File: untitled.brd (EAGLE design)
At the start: 42.2 x 28.6 mm, 27 parts, among them IC1 ACS758LCB-050B-PFF-T, IC2 LM2936DT-3.3

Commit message: Update board layout
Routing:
- net N$8: track 36.7 -> 35.9 mm
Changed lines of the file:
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@@
 <wire x1="37.465" y1="23.9219" x2="37.465" y2="24.765" width="0.3048" layer="16"/>
 <wire x1="37.465" y1="24.765" x2="37.912" y2="25.212" width="0.3048" layer="16"/>
-<wire x1="37.912" y1="25.212" x2="40.193" y2="25.212" width="0.3048" layer="16"/>
-<wire x1="40.193" y1="25.212" x2="41.275" y2="24.13" width="0.3048" layer="16"/>
-<wire x1="41.275" y1="24.13" x2="53.34" y2="24.13" width="0.3048" layer="16"/>
+<wire x1="37.912" y1="25.212" x2="38.923" y2="25.212" width="0.3048" layer="16"/>
+<wire x1="38.923" y1="25.212" x2="40.005" y2="24.13" width="0.3048" layer="16"/>
+<wire x1="40.005" y1="24.13" x2="53.34" y2="24.13" width="0.3048" layer="16"/>
 <wire x1="53.34" y1="24.13" x2="53.655" y2="23.815" width="0.3048" layer="16"/>
 <wire x1="53.655" y1="23.815" x2="53.655" y2="22.86" width="0.3048" layer="16"/>
@@
 <wire x1="45.085" y1="25.72" x2="43.18" y2="25.72" width="0.3048" layer="16"/>
 <wire x1="37.965" y1="28.1481" x2="37.965" y2="26.805" width="0.3048" layer="16"/>
-<wire x1="43.18" y1="25.72" x2="41.275" y2="25.72" width="0.4064" layer="16"/>
-<wire x1="41.275" y1="25.72" x2="40.64" y2="26.355" width="0.4064" layer="16"/>
-<wire x1="40.64" y1="26.355" x2="38.415" y2="26.355" width="0.4064" layer="16"/>
-<wire x1="38.415" y1="26.355" x2="37.965" y2="26.805" width="0.4064" layer="16"/>
+<wire x1="43.18" y1="25.72" x2="39.05" y2="25.72" width="0.4064" layer="16"/>
+<wire x1="39.05" y1="25.72" x2="37.965" y2="26.805" width="0.4064" layer="16"/>
 </signal>
 <signal name="N$1">
 <contactref element="IC1" pad="3"/>
 <contactref element="U1" pad="5"/>
-<wire x1="38.465" y1="28.1481" x2="40.4319" y2="28.1481" width="0.3048" layer="16"/>
-<wire x1="40.4319" y1="28.1481" x2="41.275" y2="27.305" width="0.4064" layer="16"/>
-<via x="41.275" y="27.305" extent="1-16" drill="0.35"/>
+<wire x1="38.465" y1="28.1481" x2="39.7969" y2="28.1481" width="0.3048" layer="16"/>
+<wire x1="39.7969" y1="28.1481" x2="41.275" y2="26.67" width="0.4064" layer="16"/>
+<via x="41.275" y="26.67" extent="1-16" drill="0.35"/>
 <via x="41.275" y="20.32" extent="1-16" drill="0.35"/>
-<wire x1="41.275" y1="20.32" x2="41.275" y2="27.305" width="0.8128" layer="1"/>
-<wire x1="39.375" y1="17.97" x2="40.645" y2="17.97" width="0.8128" layer="16"/>
-<wire x1="41.275" y1="20.32" x2="41.275" y2="18.6" width="0.8128" layer="16"/>
-<wire x1="41.275" y1="18.6" x2="40.645" y2="17.97" width="0.8128" layer="16"/>
+<wire x1="41.275" y1="20.32" x2="41.275" y2="26.67" width="0.4064" layer="1"/>
+<wire x1="39.375" y1="17.97" x2="40.645" y2="17.97" width="0.4064" layer="16"/>
+<wire x1="41.275" y1="20.32" x2="41.275" y2="18.6" width="0.4064" layer="16"/>
+<wire x1="41.275" y1="18.6" x2="40.645" y2="17.97" width="0.4064" layer="16"/>
 </signal>
 <signal name="N$4">
@@
 <wire x1="31.115" y1="38.1" x2="32.385" y2="39.37" width="0.4064" layer="1"/>
 <wire x1="31.115" y1="27.94" x2="31.115" y2="28.1714" width="0.4064" layer="1"/>
-<wire x1="31.115" y1="28.1714" x2="31.115" y2="39.37" width="0.3048" layer="1"/>
+<wire x1="31.115" y1="28.1714" x2="31.115" y2="39.37" width="0.6096" layer="1"/>
 <wire x1="31.115" y1="28.1714" x2="30.6236" y2="27.68" width="0.3048" layer="16"/>
 <wire x1="30.6236" y1="27.68" x2="28.295" y2="27.68" width="0.3048" layer="16"/>
@@
 <contactref element="Q1" pad="1"/>
 <contactref element="R8" pad="2"/>
-<wire x1="48.895" y1="27.94" x2="42.545" y2="27.94" width="0.3048" layer="1"/>
-<wire x1="42.545" y1="27.94" x2="41.91" y2="28.575" width="0.3048" layer="1"/>
-<wire x1="41.91" y1="28.575" x2="38.735" y2="28.575" width="0.3048" layer="1"/>
-<wire x1="34.29" y1="24.13" x2="38.735" y2="28.575" width="0.3048" layer="1"/>
+<wire x1="48.895" y1="27.94" x2="44.45" y2="27.94" width="0.4064" layer="1"/>
+<wire x1="44.45" y1="27.94" x2="43.815" y2="28.575" width="0.4064" layer="1"/>
+<wire x1="43.815" y1="28.575" x2="38.735" y2="28.575" width="0.4064" layer="1"/>
+<wire x1="34.29" y1="24.13" x2="38.735" y2="28.575" width="0.4064" layer="1"/>
 <wire x1="26.985" y1="20.32" x2="26.985" y2="20.635" width="0.3048" layer="16"/>
 <wire x1="26.985" y1="20.635" x2="27.94" y2="21.59" width="0.3048" layer="16"/>
@@
 <wire x1="32.385" y1="20.32" x2="33.655" y2="20.32" width="0.3048" layer="16"/>
 <wire x1="33.655" y1="20.32" x2="34.29" y2="20.955" width="0.3048" layer="16"/>
-<wire x1="34.29" y1="20.955" x2="34.29" y2="23.495" width="0.3048" layer="16"/>
-<via x="34.29" y="23.495" extent="1-16" drill="0.35"/>
-<wire x1="34.29" y1="23.495" x2="34.29" y2="24.13" width="0.3048" layer="1"/>
+<wire x1="34.29" y1="20.955" x2="34.29" y2="22.86" width="0.3048" layer="16"/>
+<via x="34.29" y="22.86" extent="1-16" drill="0.35"/>
+<wire x1="34.29" y1="22.86" x2="34.29" y2="24.13" width="0.4064" layer="1"/>
 </signal>
 <signal name="N$8">
@@
 <wire x1="31.75" y1="22.32" x2="29.17" y2="22.32" width="1.6256" layer="1"/>
 <wire x1="29.17" y1="22.32" x2="28.63" y2="22.86" width="1.27" layer="1"/>
-<wire x1="31.75" y1="22.32" x2="37.37" y2="22.32" width="0.4064" layer="1"/>
-<wire x1="37.37" y1="22.32" x2="40.64" y2="19.05" width="0.4064" layer="1"/>
-<wire x1="40.64" y1="19.05" x2="42.545" y2="19.05" width="0.4064" layer="1"/>
-<wire x1="42.545" y1="19.05" x2="43.18" y2="19.685" width="0.4064" layer="1"/>
-<wire x1="43.18" y1="19.685" x2="43.18" y2="22.86" width="0.4064" layer="1"/>
-<wire x1="43.18" y1="22.86" x2="45.72" y2="25.4" width="0.4064" layer="1"/>
-<wire x1="45.72" y1="25.4" x2="48.895" y2="25.4" width="0.4064" layer="1"/>
+<wire x1="45.085" y1="25.4" x2="42.545" y2="27.94" width="0.4064" layer="1"/>
+<wire x1="45.085" y1="25.4" x2="48.895" y2="25.4" width="0.4064" layer="1"/>
+<wire x1="39.37" y1="27.94" x2="42.545" y2="27.94" width="0.4064" layer="1"/>
+<wire x1="31.75" y1="22.32" x2="32.925" y2="22.32" width="0.4064" layer="1"/>
+<wire x1="32.925" y1="22.32" x2="33.655" y2="21.59" width="0.4064" layer="1"/>
+<wire x1="33.655" y1="21.59" x2="34.925" y2="21.59" width="0.4064" layer="1"/>
+<wire x1="34.925" y1="21.59" x2="35.56" y2="22.225" width="0.4064" layer="1"/>
+<wire x1="35.56" y1="22.225" x2="35.56" y2="24.13" width="0.4064" layer="1"/>
+<wire x1="35.56" y1="24.13" x2="39.37" y2="27.94" width="0.4064" layer="1"/>
 </signal>
 <signal name="N$12">

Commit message: Update layout
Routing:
- net GND: track 24.7 -> 16.8 mm

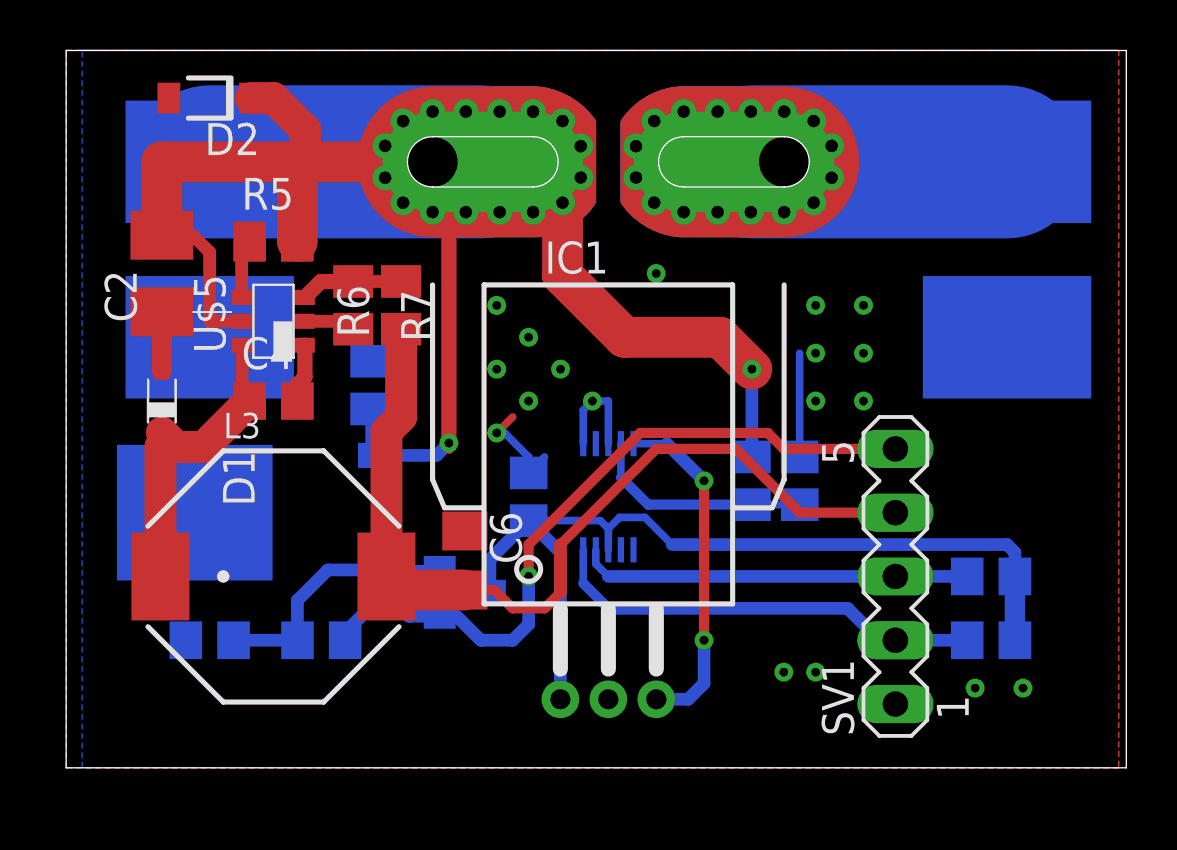
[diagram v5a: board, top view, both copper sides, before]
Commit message: Use smaller current sensor and update schematic
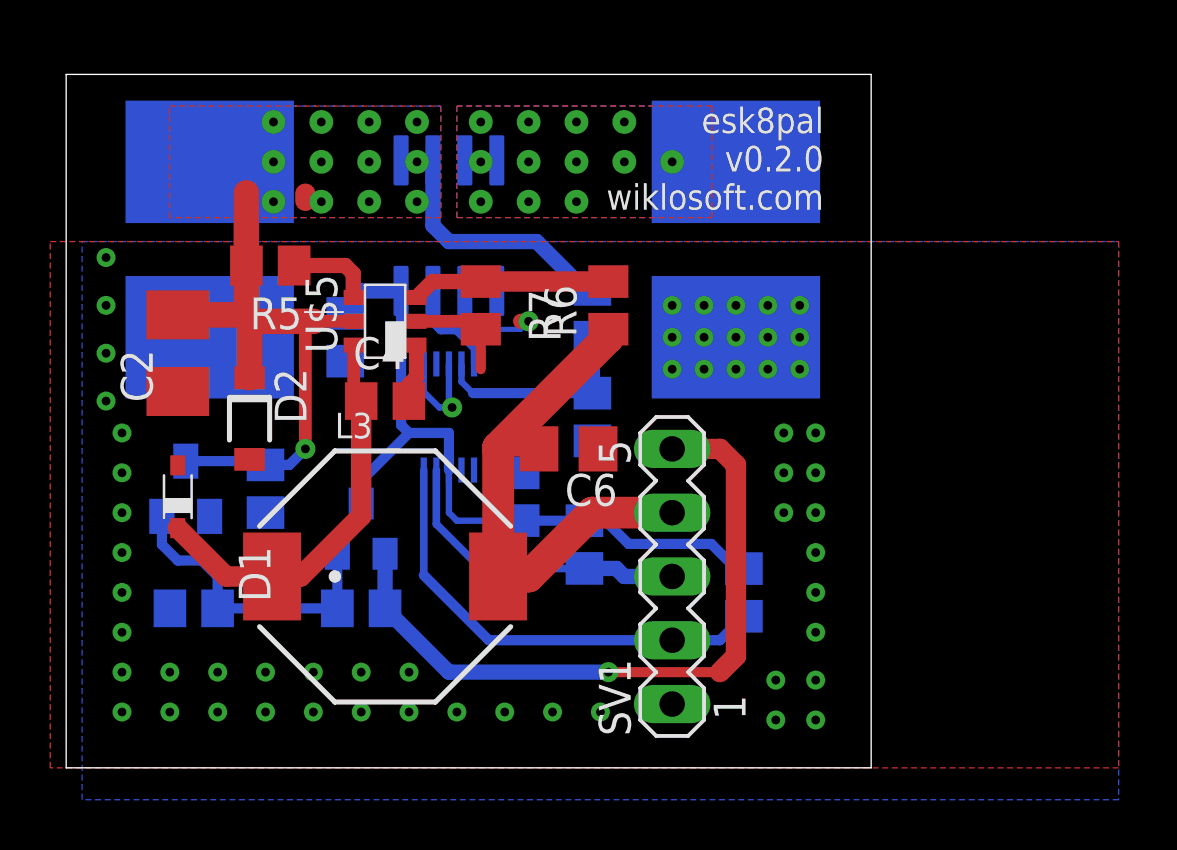
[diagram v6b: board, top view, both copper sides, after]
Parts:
- removed IC2: LM2936DT-3.3, national-semiconductor:TO252
- added C7: 100nF, rcl:C0805
- added IC3: ACS724LLCTR, we-sensor:SO08
- IC1: value ACS758LCB-050B-PFF-T -> MCP1792T-5002H/CB; device allegro:CB-PFF -> linear:SOT23
- moved IC1 21.3 mm to (20.6, 26.4), flipped to the bottom
- moved R4 16.2 mm to (36.5, 24.1), turned to 90 degrees
- moved D2 12.9 mm to (23.2, 29.1), turned to 270 degrees
- moved OUT 10.8 mm to (42.5, 39.4)
- moved U$4 10.8 mm to (42.5, 32.4)
- moved R3 10.0 mm to (42.9, 22.2), turned to 90 degrees
- moved R1 9.21 mm to (36.8, 33.3)
- moved SV1 8.89 mm to (40.0, 22.9)
- moved R2 8.64 mm to (36.8, 29.2), turned to 270 degrees
- moved R6 8.26 mm to (37.5, 33.7)
- moved U1 7.10 mm to (31.1, 29.2)
- moved C6 6.07 mm to (35.9, 27.9), turned to 180 degrees
- moved C5 5.84 mm to (23.8, 26.4), turned to 270 degrees
- moved R7 5.08 mm to (32.4, 33.7)
- moved Q1 4.85 mm to (27.6, 24.8), turned to 0 degrees
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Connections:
- net GND: now also C7.2, IC1.1, IC3.5; no longer IC1.2, IC2.2
- net N$1: now also IC3.7; no longer IC1.3
- net N$12: now also IC1.2; no longer IC2.3
- net N$2: now also IC3.3, IC3.4; no longer IC1.IP+, IC1.IP+@10, IC1.IP+@11, IC1.IP+@12, IC1.IP+@13, IC1.IP+@14, IC1.IP+@15, IC1.IP+@16, IC1.IP+@17, IC1.IP+@2, IC1.IP+@3, IC1.IP+@4, IC1.IP+@5, IC1.IP+@6, IC1.IP+@7, IC1.IP+@8, IC1.IP+@9
- net N$4: now also IC1.3, IC3.1, IC3.2; no longer IC1.IP-, IC1.IP-@10, IC1.IP-@11, IC1.IP-@12, IC1.IP-@13, IC1.IP-@14, IC1.IP-@15, IC1.IP-@16, IC1.IP-@17, IC1.IP-@2, IC1.IP-@3, IC1.IP-@4, IC1.IP-@5, IC1.IP-@6, IC1.IP-@7, IC1.IP-@8, IC1.IP-@9, IC2.1
- net VCC: now also C7.1, IC3.8; no longer IC1.1
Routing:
- net N$4: track 89.2 -> 35.3 mm, vias 2 -> 13
- net N$8: track 35.9 -> 21.3 mm
- net N$2: track 10.2 -> 0.08 mm, vias 0 -> 12
- net N$1: track 13.7 -> 4.53 mm, vias 2 -> 0
- net VCC: track 37.2 -> 30.0 mm
- net GND: track 16.8 -> 11.8 mm, vias 18 -> 58
- net N$11: track 4.09 -> 7.90 mm
- net N$9: track 12.6 -> 16.1 mm
- net N$5: track 15.6 -> 12.4 mm
- net N$12: track 10.3 -> 12.1 mm
- net N$3: track 2.37 -> 3.45 mm
- net N$6: track 17.6 -> 18.4 mm
- net N$7: track 28.7 -> 27.9 mm
- added copper zone on layer 1, net N$2
- added copper zone on layer 16, net N$2
- added copper zone on layer 1, net N$4
- added copper zone on layer 16, net N$4
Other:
- board size 42.2 x 28.6 mm -> 32.1 x 27.6 mm
- board text added: "esk8pal v0.2.0 wiklosoft.com"
- board text removed: "esk8pal v0.1.0 wiklosoft.com"
